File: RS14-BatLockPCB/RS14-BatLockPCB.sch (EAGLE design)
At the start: 19 parts, among them IC1 LM741D, Q1 2N3904

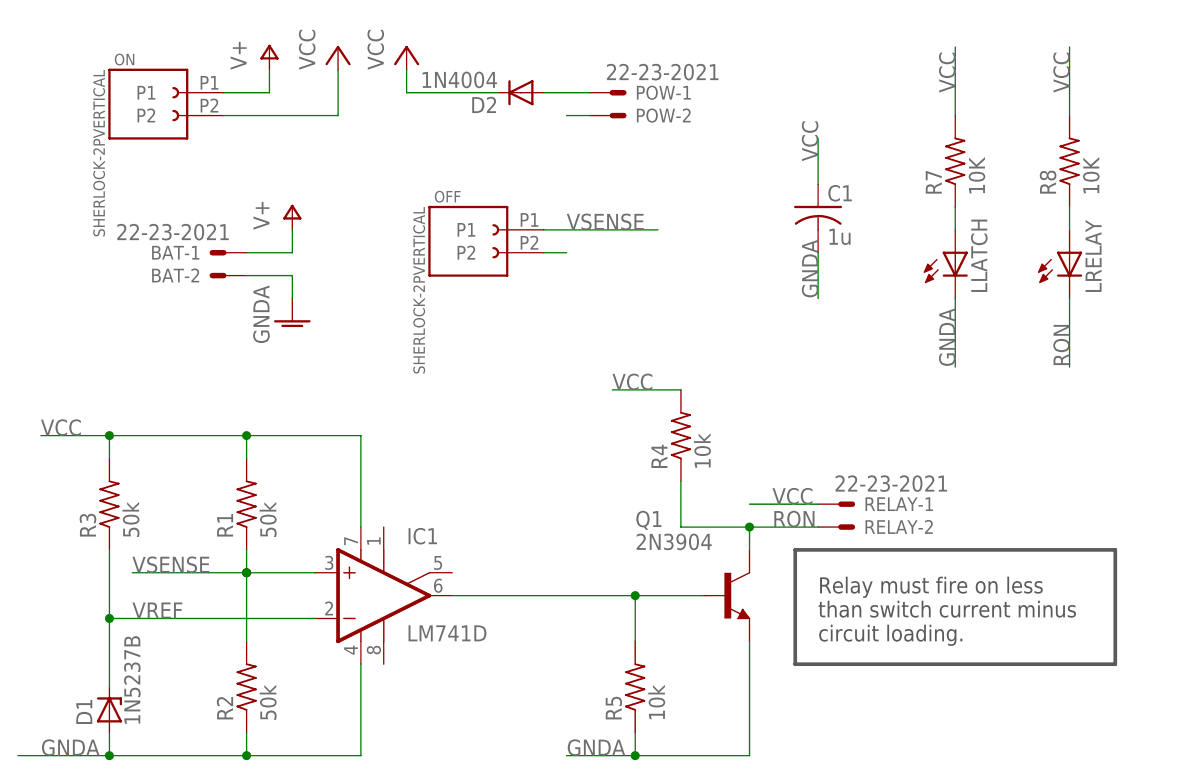
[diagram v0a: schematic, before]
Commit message: Updated layouts for new hole sizes
Updated both boards to include proper sized holes for the screws (correction from 0.22" radius to 0.22" diamater clearance). This also includes some minor tweeks to clean up the board size a bit.
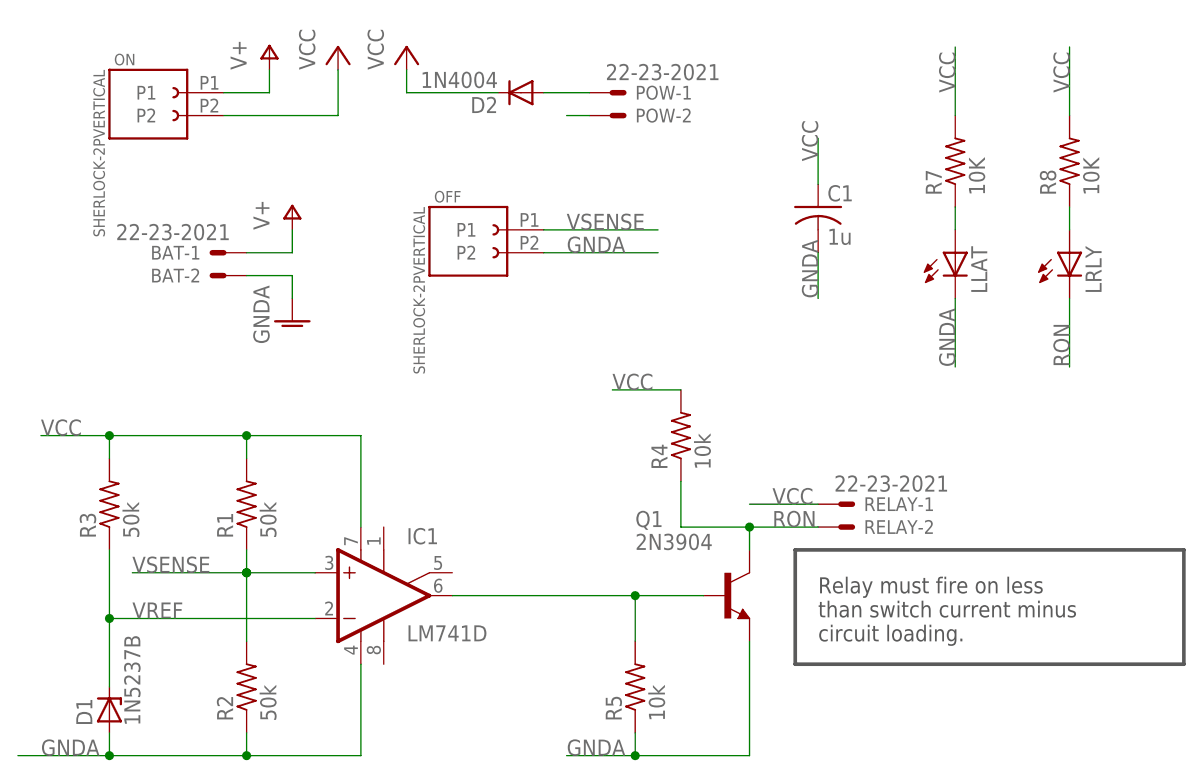
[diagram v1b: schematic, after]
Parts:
- renumbered LLATCH to LLAT, LRELAY to LRLY
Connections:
- removed net N$3: OFF.P2
- net GNDA: now also OFF.P2
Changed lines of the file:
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@@
 <part name="R7" library="rcl" deviceset="R-US_" device="0204/7" value="10K"/>
 <part name="R8" library="rcl" deviceset="R-US_" device="0204/7" value="10K"/>
-<part name="LLATCH" library="led" deviceset="LED" device="3MM"/>
-<part name="LRELAY" library="led" deviceset="LED" device="3MM"/>
+<part name="LLAT" library="led" deviceset="LED" device="3MM"/>
+<part name="LRLY" library="led" deviceset="LED" device="3MM"/>
 </parts>
 <sheets>
@@
 than switch current minus
 circuit loading.</text>
-<wire x1="96.52" y1="22.86" x2="132.08" y2="22.86" width="0.4064" layer="97"/>
-<wire x1="132.08" y1="22.86" x2="132.08" y2="10.16" width="0.4064" layer="97"/>
-<wire x1="132.08" y1="10.16" x2="96.52" y2="10.16" width="0.4064" layer="97"/>
+<wire x1="96.52" y1="22.86" x2="139.7" y2="22.86" width="0.4064" layer="97"/>
+<wire x1="139.7" y1="22.86" x2="139.7" y2="10.16" width="0.4064" layer="97"/>
+<wire x1="139.7" y1="10.16" x2="96.52" y2="10.16" width="0.4064" layer="97"/>
 <wire x1="96.52" y1="10.16" x2="96.52" y2="22.86" width="0.4064" layer="97"/>
 </plain>
@@
 <instance part="R7" gate="G$1" x="114.3" y="66.04" rot="R90"/>
 <instance part="R8" gate="G$1" x="127" y="66.04" rot="R90"/>
-<instance part="LLATCH" gate="G$1" x="114.3" y="55.88"/>
-<instance part="LRELAY" gate="G$1" x="127" y="55.88"/>
+<instance part="LLAT" gate="G$1" x="114.3" y="55.88"/>
+<instance part="LRLY" gate="G$1" x="127" y="55.88"/>
 </instances>
 <busses>
@@
 </segment>
 <segment>
-<pinref part="LLATCH" gate="G$1" pin="C"/>
+<pinref part="LLAT" gate="G$1" pin="C"/>
 <wire x1="114.3" y1="50.8" x2="114.3" y2="43.18" width="0.1524" layer="91"/>
 <label x="114.3" y="43.18" size="1.778" layer="95" rot="R90"/>
@@
 <label x="71.12" y="0" size="1.778" layer="95"/>
 </segment>
+<segment>
+<pinref part="OFF" gate="G$1" pin="P2"/>
+<wire x1="68.58" y1="55.88" x2="81.28" y2="55.88" width="0.1524" layer="91"/>
+<label x="71.12" y="55.88" size="1.778" layer="95"/>
+</segment>
 </net>
 <net name="VCC" class="0">
@@
 </segment>
 <segment>
-<pinref part="LRELAY" gate="G$1" pin="C"/>
+<pinref part="LRLY" gate="G$1" pin="C"/>
 <wire x1="127" y1="50.8" x2="127" y2="43.18" width="0.1524" layer="91"/>
 <label x="127" y="43.18" size="1.778" layer="95" rot="R90"/>
@@
 <net name="N$7" class="0">
 <segment>
-<pinref part="LLATCH" gate="G$1" pin="A"/>
+<pinref part="LLAT" gate="G$1" pin="A"/>
 <pinref part="R7" gate="G$1" pin="1"/>
 <wire x1="114.3" y1="58.42" x2="114.3" y2="60.96" width="0.1524" layer="91"/>
@@
 <net name="N$8" class="0">
 <segment>
-<pinref part="LRELAY" gate="G$1" pin="A"/>
+<pinref part="LRLY" gate="G$1" pin="A"/>
 <pinref part="R8" gate="G$1" pin="1"/>
 <wire x1="127" y1="58.42" x2="127" y2="60.96" width="0.1524" layer="91"/>
@@
 </segment>
 </net>
-<net name="N$3" class="0">
-<segment>
-<pinref part="OFF" gate="G$1" pin="P2"/>
-<wire x1="68.58" y1="55.88" x2="71.12" y2="55.88" width="0.1524" layer="91"/>
-</segment>
-</net>
